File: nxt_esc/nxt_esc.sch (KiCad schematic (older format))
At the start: 21 parts, among them IC1 L293D, J1 NXT_MOTOR, J2 NXT_MOTOR, SW1 Skid Steer/Drive & Steer, U1 LM7805CT

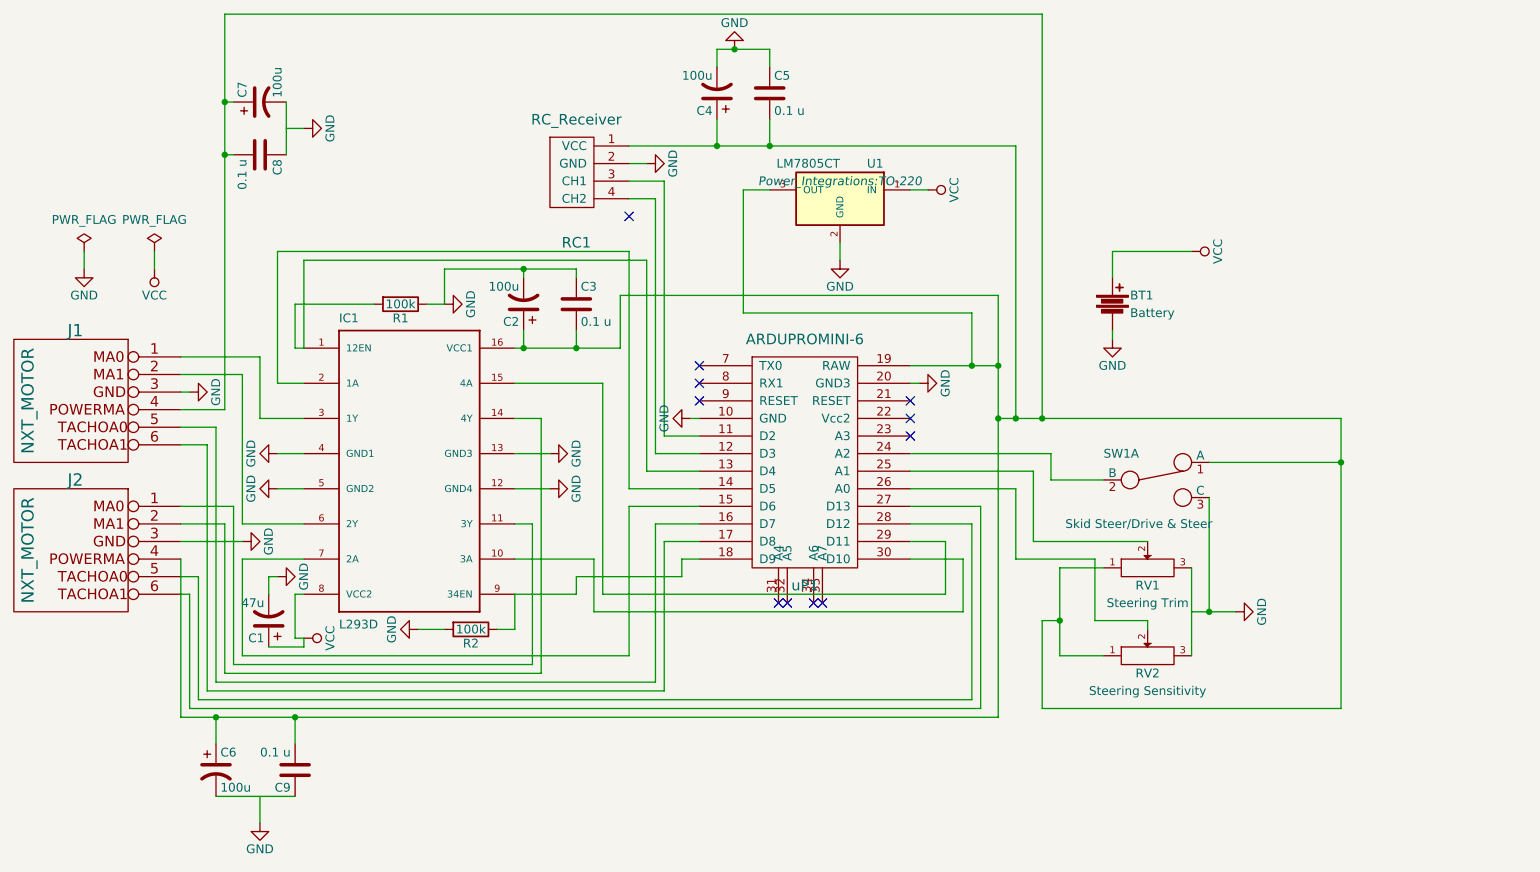
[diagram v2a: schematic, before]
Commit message: Resized board to 6x6 Lego size
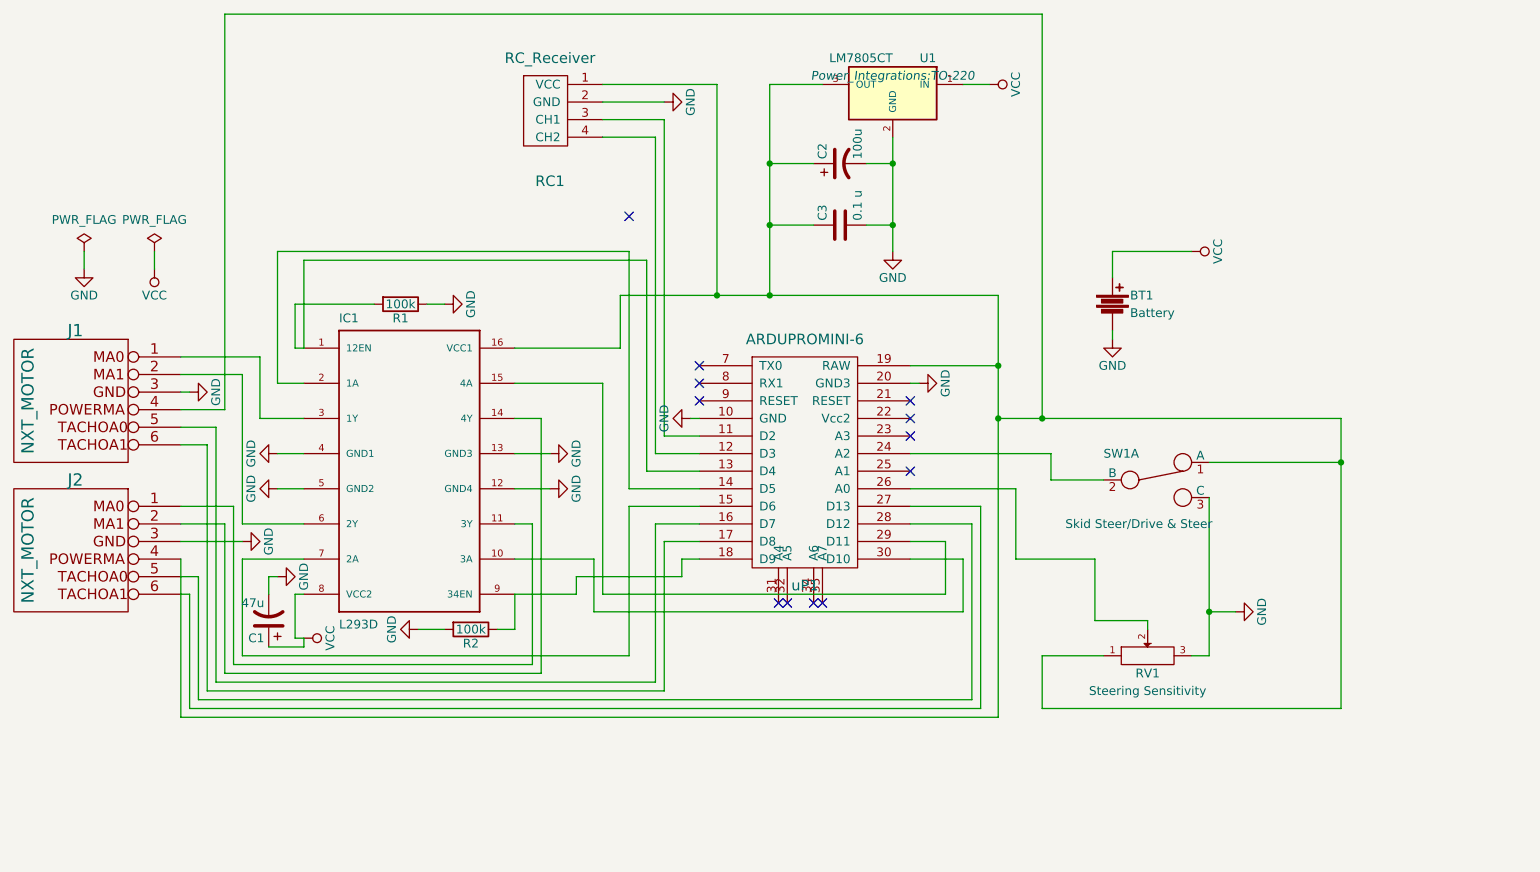
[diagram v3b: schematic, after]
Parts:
- removed C2, C6, C7: 100u, Capacitors_ThroughHole:CP_Radial_D5.0mm_P2.50mm, symbol CP1
- removed C3, C8, C9: 0.1 u, Capacitors_ThroughHole:C_Disc_D3.4mm_W2.1mm_P2.50mm, symbol C
- removed RV1: Steering Trim, Potentiometers:Potentiometer_Trimmer_ACP_CA6v_Horizontal, symbol POT
- renumbered C4 to C2, C5 to C3, RV2 to RV1
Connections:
- net GND: now also C3.2, RV1.3; no longer C3.1
- net at C2.1, IC1.16 (VCC1), J1.4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: now also C3.1; no longer C3.2
- no-connect marks 11 -> 12
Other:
- moved on the sheet: C2, C3, RC1, U1

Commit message: Added center steering button
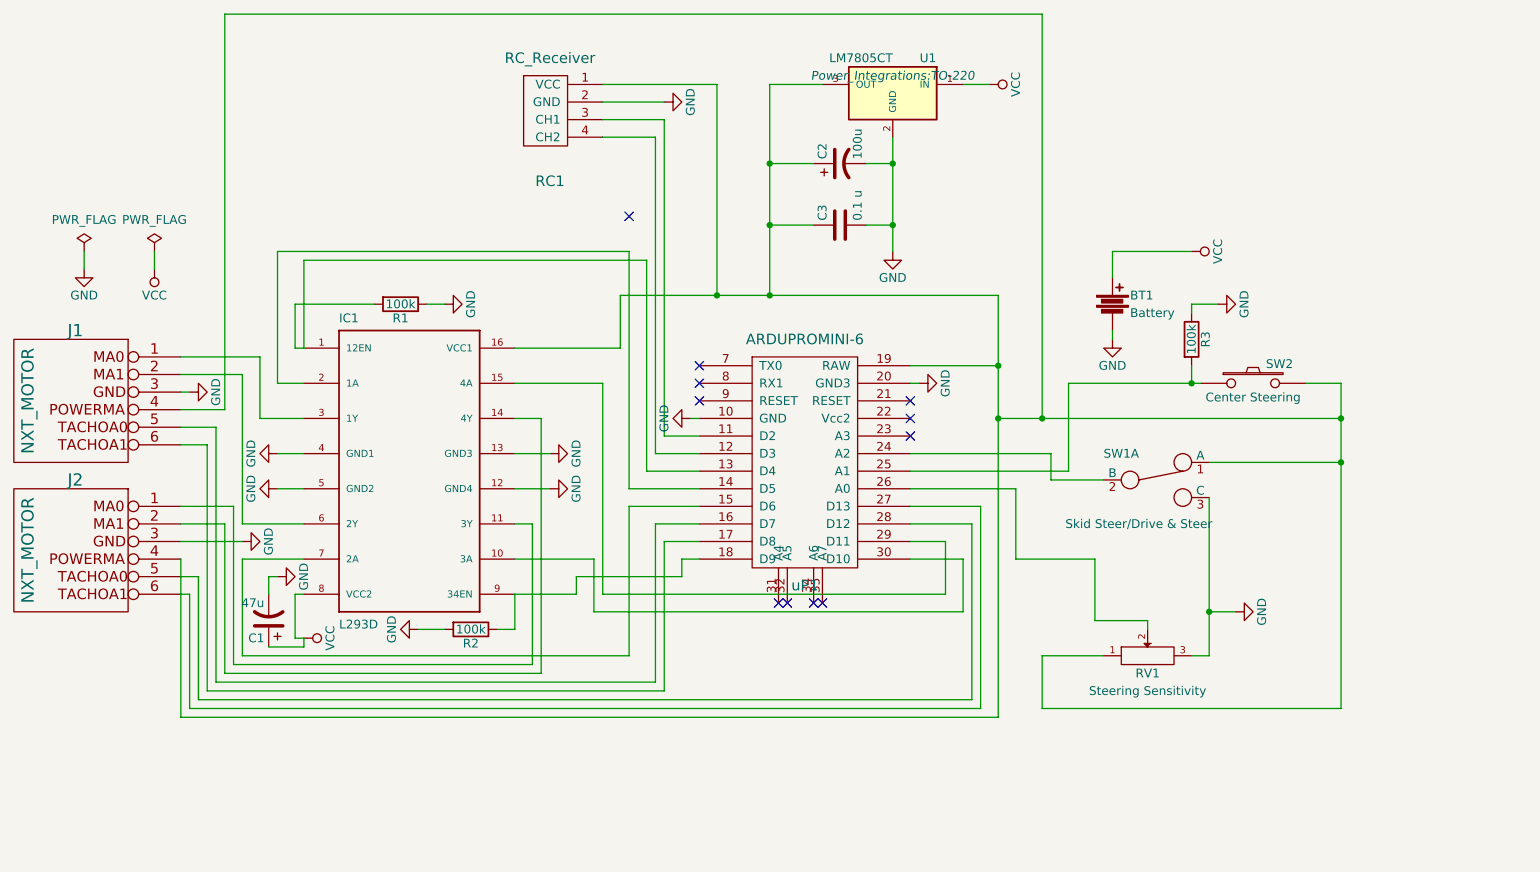
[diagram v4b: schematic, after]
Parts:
- added R3: 100k, Resistors_ThroughHole:R_Axial_DIN0204_L3.6mm_D1.6mm_P7.62mm_Horizontal, symbol R
- added SW2: Center Steering, Buttons_Switches_ThroughHole:SW_PUSH_6mm, symbol SW_PUSH
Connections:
- net GND: now also R3.1
- net at C2.1, C3.1, IC1.16 (VCC1)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: now also SW2.2
- net at uP1.25 (A1): now also R3.2, SW2.1
- no-connect marks 12 -> 11
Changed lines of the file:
@@
 NoConn ~ 5700 3300
 $Comp
-L GND #PWR5
+L GND #PWR01
 U 1 1 5A5529EC
 P 3300 3600
-F 0 "#PWR5" H 3300 3350 50  0001 C CNN
+F 0 "#PWR01" H 3300 3350 50  0001 C CNN
 F 1 "GND" H 3300 3450 50  0000 C CNN
 F 2 "" H 3300 3600 50  0000 C CNN
@@
 $EndComp
 $Comp
-L GND #PWR11
+L GND #PWR02
 U 1 1 5A552A37
 P 4850 3600
-F 0 "#PWR11" H 4850 3350 50  0001 C CNN
+F 0 "#PWR02" H 4850 3350 50  0001 C CNN
 F 1 "GND" H 4850 3450 50  0000 C CNN
 F 2 "" H 4850 3600 50  0000 C CNN
@@
 $EndComp
 $Comp
-L GND #PWR12
+L GND #PWR03
 U 1 1 5A552A75
 P 4850 3800
-F 0 "#PWR12" H 4850 3550 50  0001 C CNN
+F 0 "#PWR03" H 4850 3550 50  0001 C CNN
 F 1 "GND" H 4850 3650 50  0000 C CNN
 F 2 "" H 4850 3800 50  0000 C CNN
@@
 $EndComp
 $Comp
-L GND #PWR16
+L GND #PWR04
 U 1 1 5A552A8F
 P 6950 3200
-F 0 "#PWR16" H 6950 2950 50  0001 C CNN
+F 0 "#PWR04" H 6950 2950 50  0001 C CNN
 F 1 "GND" H 6950 3050 50  0000 C CNN
 F 2 "" H 6950 3200 50  0000 C CNN
@@
 $EndComp
 $Comp
-L GND #PWR14
+L GND #PWR05
 U 1 1 5A552AA9
 P 5650 3400
-F 0 "#PWR14" H 5650 3150 50  0001 C CNN
+F 0 "#PWR05" H 5650 3150 50  0001 C CNN
 F 1 "GND" H 5650 3250 50  0000 C CNN
 F 2 "" H 5650 3400 50  0000 C CNN
@@
 $EndComp
 $Comp
-L GND #PWR13
+L GND #PWR06
 U 1 1 5A552D75
 P 5500 1600
-F 0 "#PWR13" H 5500 1350 50  0001 C CNN
+F 0 "#PWR06" H 5500 1350 50  0001 C CNN
 F 1 "GND" H 5500 1450 50  0000 C CNN
 F 2 "" H 5500 1600 50  0000 C CNN
@@
 NoConn ~ 6900 3300
 $Comp
-L GND #PWR6
+L GND #PWR07
 U 1 1 5A554D29
 P 3300 3800
-F 0 "#PWR6" H 3300 3550 50  0001 C CNN
+F 0 "#PWR07" H 3300 3550 50  0001 C CNN
 F 1 "GND" H 3300 3650 50  0000 C CNN
 F 2 "" H 3300 3800 50  0000 C CNN
@@
 $EndComp
 $Comp
-L GND #PWR3
+L GND #PWR08
 U 1 1 5A555011
 P 2800 3250
-F 0 "#PWR3" H 2800 3000 50  0001 C CNN
+F 0 "#PWR08" H 2800 3000 50  0001 C CNN
 F 1 "GND" H 2800 3100 50  0000 C CNN
 F 2 "" H 2800 3250 50  0000 C CNN
@@
 $EndComp
 $Comp
-L GND #PWR4
+L GND #PWR09
 U 1 1 5A555143
 P 3100 4100
-F 0 "#PWR4" H 3100 3850 50  0001 C CNN
+F 0 "#PWR09" H 3100 3850 50  0001 C CNN
 F 1 "GND" H 3100 3950 50  0000 C CNN
 F 2 "" H 3100 4100 50  0000 C CNN
@@
 $EndComp
 $Comp
-L PWR_FLAG #FLG1
+L PWR_FLAG #FLG010
 U 1 1 5A555514
 P 2200 2450
-F 0 "#FLG1" H 2200 2545 50  0001 C CNN
+F 0 "#FLG010" H 2200 2545 50  0001 C CNN
 F 1 "PWR_FLAG" H 2200 2630 50  0000 C CNN
 F 2 "" H 2200 2450 50  0000 C CNN
@@
 $EndComp
 $Comp
-L GND #PWR1
+L GND #PWR011
 U 1 1 5A555531
 P 2200 2550
-F 0 "#PWR1" H 2200 2300 50  0001 C CNN
+F 0 "#PWR011" H 2200 2300 50  0001 C CNN
 F 1 "GND" H 2200 2400 50  0000 C CNN
 F 2 "" H 2200 2550 50  0000 C CNN
@@
 $EndComp
 $Comp
-L VCC #PWR8
+L VCC #PWR012
 U 1 1 5A555A79
 P 3450 4650
-F 0 "#PWR8" H 3450 4500 50  0001 C CNN
+F 0 "#PWR012" H 3450 4500 50  0001 C CNN
 F 1 "VCC" H 3450 4800 50  0000 C CNN
 F 2 "" H 3450 4650 50  0000 C CNN
@@
 $EndComp
 $Comp
-L GND #PWR10
+L GND #PWR013
 U 1 1 5A554FA2
 P 4250 2750
-F 0 "#PWR10" H 4250 2500 50  0001 C CNN
+F 0 "#PWR013" H 4250 2500 50  0001 C CNN
 F 1 "GND" H 4250 2600 50  0000 C CNN
 F 2 "" H 4250 2750 50  0000 C CNN
@@
 $EndComp
 $Comp
-L GND #PWR9
+L GND #PWR014
 U 1 1 5A5551A8
 P 4100 4600
-F 0 "#PWR9" H 4100 4350 50  0001 C CNN
+F 0 "#PWR014" H 4100 4350 50  0001 C CNN
 F 1 "GND" H 4100 4450 50  0000 C CNN
 F 2 "" H 4100 4600 50  0000 C CNN
@@
 $EndComp
 $Comp
-L GND #PWR7
+L GND #PWR015
 U 1 1 5A5557E8
 P 3300 4300
-F 0 "#PWR7" H 3300 4050 50  0001 C CNN
+F 0 "#PWR015" H 3300 4050 50  0001 C CNN
 F 1 "GND" H 3300 4150 50  0000 C CNN
 F 2 "" H 3300 4300 50  0000 C CNN
@@
 	2750 4200 2750 5100
 Wire Wire Line
-	7400 5100 2750 5100
+	2750 5100 7400 5100
 Wire Wire Line
 	4650 3000 5250 3000
@@
 	3450 4650 3400 4650
 $Comp
-L VCC #PWR19
+L VCC #PWR016
 U 1 1 5A556AED
 P 8500 2450
-F 0 "#PWR19" H 8500 2300 50  0001 C CNN
+F 0 "#PWR016" H 8500 2300 50  0001 C CNN
 F 1 "VCC" H 8500 2600 50  0000 C CNN
 F 2 "" H 8500 2450 50  0000 C CNN
@@
 $EndComp
 $Comp
-L GND #PWR18
+L GND #PWR017
 U 1 1 5A556F7B
 P 8050 2950
-F 0 "#PWR18" H 8050 2700 50  0001 C CNN
+F 0 "#PWR017" H 8050 2700 50  0001 C CNN
 F 1 "GND" H 8050 2800 50  0000 C CNN
 F 2 "" H 8050 2950 50  0000 C CNN
@@
 $EndComp
 $Comp
-L GND #PWR20
+L GND #PWR018
 U 1 1 5A55820D
 P 8750 4500
-F 0 "#PWR20" H 8750 4250 50  0001 C CNN
+F 0 "#PWR018" H 8750 4250 50  0001 C CNN
 F 1 "GND" H 8750 4350 50  0000 C CNN
 F 2 "" H 8750 4500 50  0000 C CNN
@@
 	9350 5050 7650 5050
 Wire Wire Line
-	9350 3400 9350 5050
+	9350 3200 9350 5050
 Connection ~ 9350 3650
 Connection ~ 7650 3400
@@
 $EndComp
 $Comp
-L GND #PWR15
+L GND #PWR019
 U 1 1 5A56A814
 P 6800 2450
-F 0 "#PWR15" H 6800 2200 50  0001 C CNN
+F 0 "#PWR019" H 6800 2200 50  0001 C CNN
 F 1 "GND" H 6800 2300 50  0000 C CNN
 F 2 "" H 6800 2450 50  0000 C CNN
@@
 	6800 1800 6800 2450
 $Comp
-L VCC #PWR17
+L VCC #PWR020
 U 1 1 5A56A933
 P 7350 1500
-F 0 "#PWR17" H 7350 1350 50  0001 C CNN
+F 0 "#PWR020" H 7350 1350 50  0001 C CNN
 F 1 "VCC" H 7350 1650 50  0000 C CNN
 F 2 "" H 7350 1500 50  0000 C CNN
@@
 Connection ~ 7400 3100
 $Comp
-L PWR_FLAG #FLG2
+L PWR_FLAG #FLG021
 U 1 1 5A56B6A2
 P 2600 2450
-F 0 "#FLG2" H 2600 2545 50  0001 C CNN
+F 0 "#FLG021" H 2600 2545 50  0001 C CNN
 F 1 "PWR_FLAG" H 2600 2630 50  0000 C CNN
 F 2 "" H 2600 2450 50  0000 C CNN
@@
 $EndComp
 $Comp
-L VCC #PWR2
+L VCC #PWR022
 U 1 1 5A56B6DA
 P 2600 2550
-F 0 "#PWR2" H 2600 2400 50  0001 C CNN
+F 0 "#PWR022" H 2600 2400 50  0001 C CNN
 F 1 "VCC" H 2600 2700 50  0000 C CNN
 F 2 "" H 2600 2550 50  0000 C CNN
@@
 Wire Wire Line
 	8600 4500 8750 4500
-NoConn ~ 6900 3700
 Wire Wire Line
 	6400 1500 6100 1500
@@
 	5800 1500 5800 2700
 Connection ~ 5800 2700
+$Comp
+L SW_PUSH SW2
+U 1 1 5AA99BAD
+P 8850 3200
+F 0 "SW2" H 9000 3310 50  0000 C CNN
+F 1 "Center Steering" H 8850 3120 50  0000 C CNN
+F 2 "Buttons_Switches_ThroughHole:SW_PUSH_6mm" H 8850 3200 50  0001 C CNN
+F 3 "" H 8850 3200 50  0000 C CNN
+	1    8850 3200
+	1    0    0    -1
+$EndComp
+$Comp
+L R R3
+U 1 1 5AA99C24
+P 8500 2950
+F 0 "R3" V 8580 2950 50  0000 C CNN
+F 1 "100k" V 8500 2950 50  0000 C CNN
+F 2 "Resistors_ThroughHole:R_Axial_DIN0204_L3.6mm_D1.6mm_P7.62mm_Horizontal" V 8430 2950 50  0001 C CNN
+F 3 "" H 8500 2950 50  0000 C CNN
+	1    8500 2950
+	1    0    0    -1
+$EndComp
+$Comp
+L GND #PWR023
+U 1 1 5AA99CCB
+P 8650 2750
+F 0 "#PWR023" H 8650 2500 50  0001 C CNN
+F 1 "GND" H 8650 2600 50  0000 C CNN
+F 2 "" H 8650 2750 50  0000 C CNN
+F 3 "" H 8650 2750 50  0000 C CNN
+	1    8650 2750
+	0    -1   1    0
+$EndComp
+Wire Wire Line
+	8650 2750 8500 2750
+Wire Wire Line
+	8500 2750 8500 2800
+Wire Wire Line
+	9150 3200 9350 3200
+Connection ~ 9350 3400
+Wire Wire Line
+	8550 3200 7800 3200
+Wire Wire Line
+	7800 3200 7800 3700
+Wire Wire Line
+	7800 3700 6900 3700
+Wire Wire Line
+	8500 3100 8500 3200
+Connection ~ 8500 3200
 $EndSCHEMATC

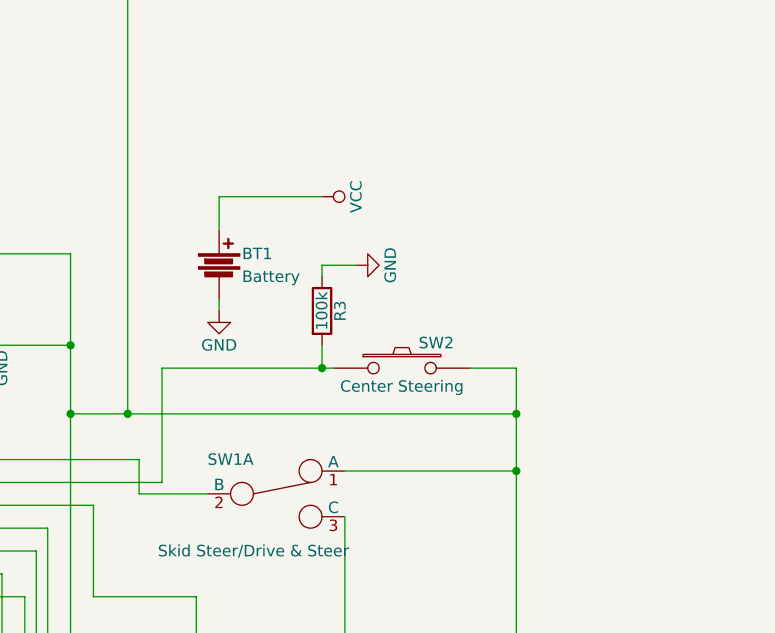
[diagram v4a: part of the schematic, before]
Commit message: Added reverse polarity protection diode and power switch
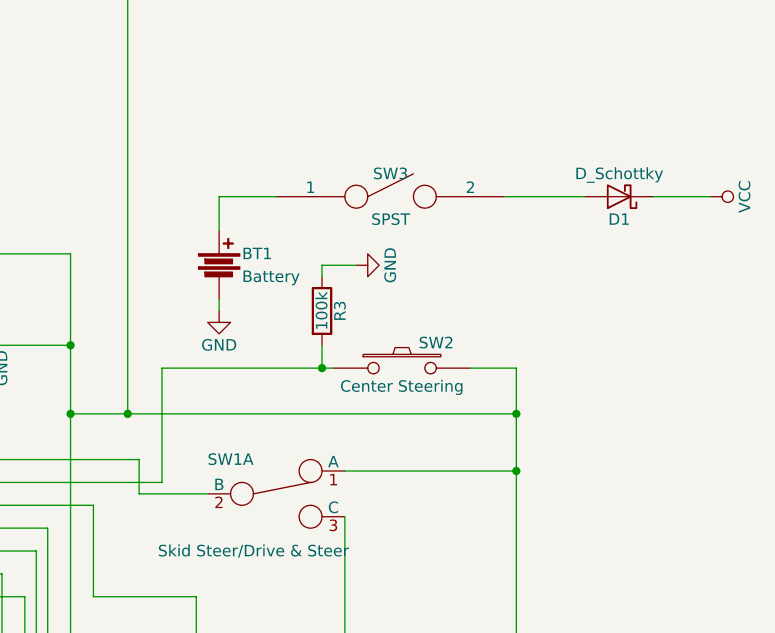
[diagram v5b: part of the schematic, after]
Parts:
- added D1: D_Schottky, Diodes_ThroughHole:D_A-405_P10.16mm_Horizontal, symbol D_Schottky
- added SW3: SPST, Buttons_Switches_ThroughHole:SW_DIP_x1_W7.62mm_Slide, symbol SPST
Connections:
- net VCC: now also D1.1 (K); no longer BT1.1
- new net: BT1.1, SW3.1
- new net: D1.2 (A), SW3.2
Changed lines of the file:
@@
 L VCC #PWR016
 U 1 1 5A556AED
-P 8500 2450
-F 0 "#PWR016" H 8500 2300 50  0001 C CNN
-F 1 "VCC" H 8500 2600 50  0000 C CNN
-F 2 "" H 8500 2450 50  0000 C CNN
-F 3 "" H 8500 2450 50  0000 C CNN
-	1    8500 2450
+P 10200 2450
+F 0 "#PWR016" H 10200 2300 50  0001 C CNN
+F 1 "VCC" H 10200 2600 50  0000 C CNN
+F 2 "" H 10200 2450 50  0000 C CNN
+F 3 "" H 10200 2450 50  0000 C CNN
+	1    10200 2450
 	0    1    1    0
 $EndComp
@@
 Connection ~ 8600 4500
 Wire Wire Line
-	8600 3650 9350 3650
+	9350 3650 8600 3650
 Wire Wire Line
 	7650 4750 8000 4750
@@
 Wire Wire Line
 	8050 2600 8050 2450
-Wire Wire Line
-	8050 2450 8500 2450
 $Comp
 L LM7805CT U1
@@
 Connection ~ 9350 3400
 Wire Wire Line
-	8550 3200 7800 3200
+	7800 3200 8550 3200
 Wire Wire Line
 	7800 3200 7800 3700
@@
 	8500 3100 8500 3200
 Connection ~ 8500 3200
+$Comp
+L D_Schottky D1
+U 1 1 5AABEECE
+P 9800 2450
+F 0 "D1" H 9800 2550 50  0000 C CNN
+F 1 "D_Schottky" H 9800 2350 50  0000 C CNN
+F 2 "Diodes_ThroughHole:D_A-405_P10.16mm_Horizontal" H 9800 2450 50  0001 C CNN
+F 3 "" H 9800 2450 50  0000 C CNN
+	1    9800 2450
+	-1   0    0    1
+$EndComp
+$Comp
+L SPST SW3
+U 1 1 5AABF253
+P 8800 2450
+F 0 "SW3" H 8800 2550 50  0000 C CNN
+F 1 "SPST" H 8800 2350 50  0000 C CNN
+F 2 "Buttons_Switches_ThroughHole:SW_DIP_x1_W7.62mm_Slide" H 8800 2450 50  0001 C CNN
+F 3 "" H 8800 2450 50  0000 C CNN
+	1    8800 2450
+	1    0    0    -1
+$EndComp
+Wire Wire Line
+	8050 2450 8300 2450
+Wire Wire Line
+	9300 2450 9650 2450
+Wire Wire Line
+	9950 2450 10200 2450
 $EndSCHEMATC
